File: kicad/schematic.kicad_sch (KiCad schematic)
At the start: 22 parts, among them J1 16X02 LCD Display I2C, J2 500g. Load Cell Sensor, J3 NAU7802, 24-Bit Dual-Channel.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, J4 TP4056 Lithium Battery Chargi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, SW1 Tare, SW2 Power Switch, SW3 Up, SW4 Down, SW5 Enter, SW6 Cancel, SW7 Coffee, U1 Step-up DC-to-DC 0.9-5V to 5V

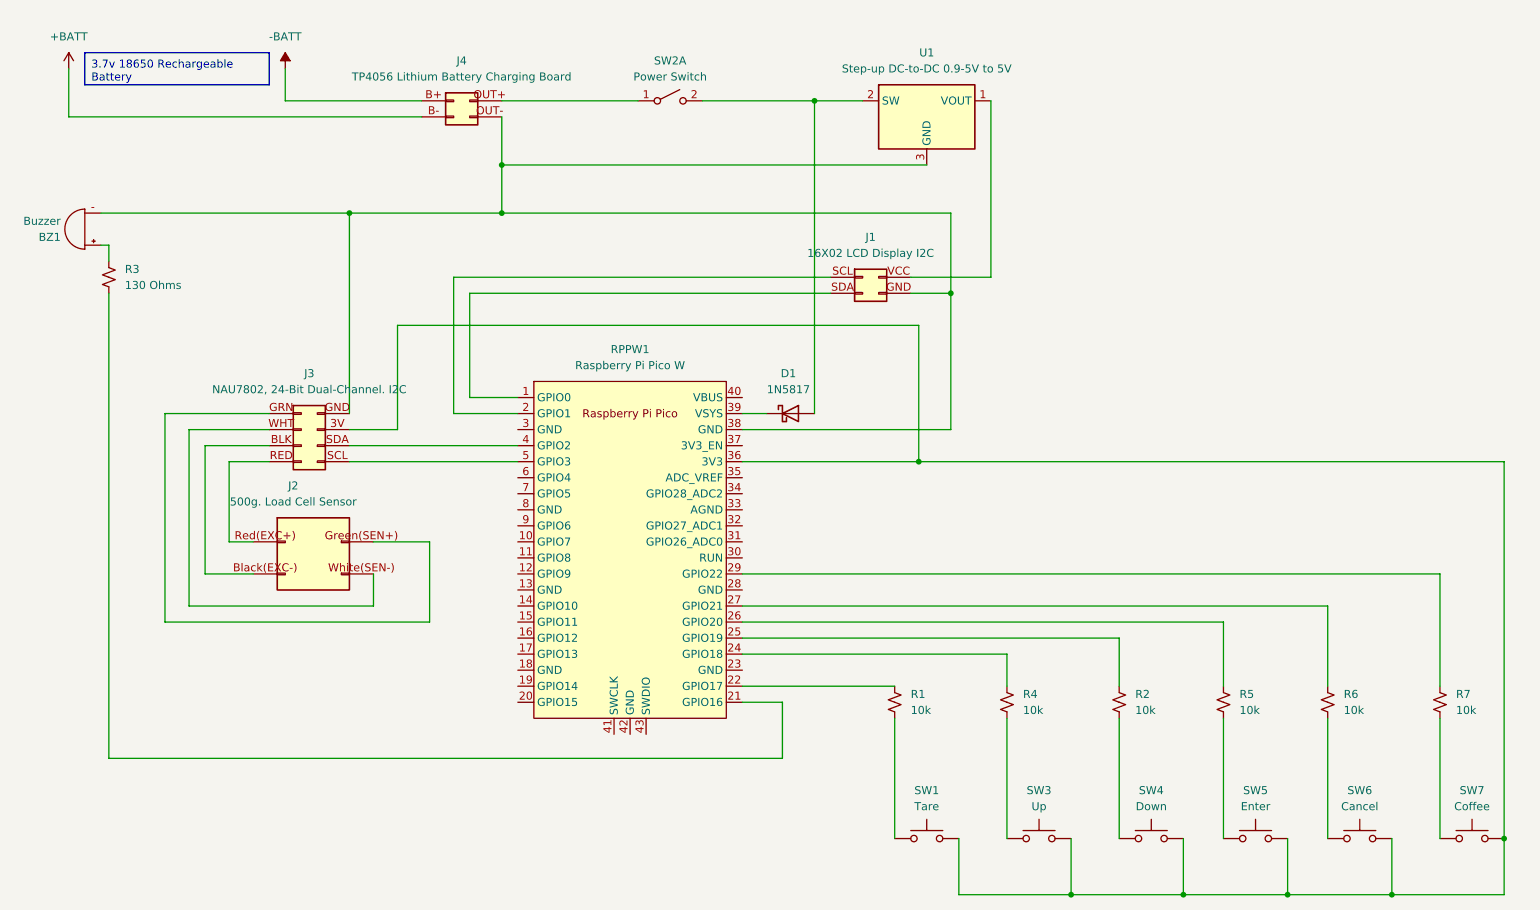
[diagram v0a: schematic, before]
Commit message: fix schematic buttons
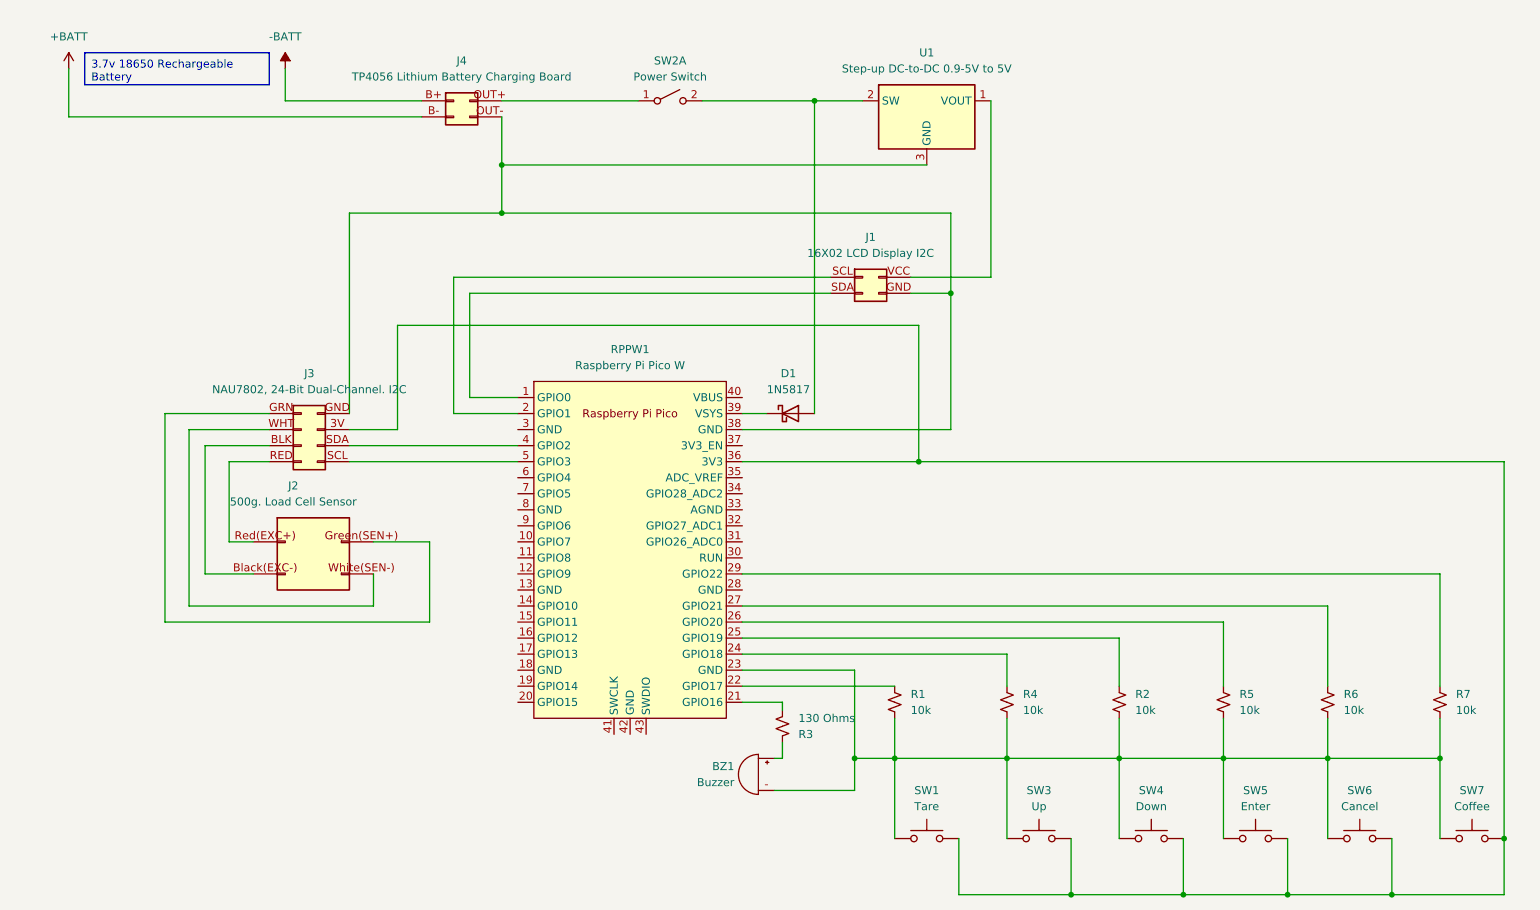
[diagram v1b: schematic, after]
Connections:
- net at J1.GND (Pin_3), J3.GND (Pin_8), J4.OUT- (Pin_3)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: no longer BZ1.-
- net at R2.2, SW4.1 (A), SW4.2 (A): now also BZ1.-, R1.2, R4.2, R5.2, R6.2, R7.2, RPPW1.23 (GND), SW1.1 (A), SW1.2 (A), SW3.1 (A), SW3.2 (A), SW5.1 (A), SW5.2 (A), SW6.1 (A), SW6.2 (A), SW7.1 (A), SW7.2 (A)
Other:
- moved on the sheet: BZ1, R3
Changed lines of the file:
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@@
   (junction (at 158.75 85.09) (diameter 0) (color 0 0 0 0)
   )
+  (junction (at 190.5 132.08) (diameter 0) (color 0 0 0 0)
+  )
+  (junction (at 241.3 132.08) (diameter 0) (color 0 0 0 0)
+  )
   (junction (at 182.88 153.67) (diameter 0) (color 0 0 0 0)
   )
+  (junction (at 207.01 132.08) (diameter 0) (color 0 0 0 0)
+  )
+  (junction (at 172.72 132.08) (diameter 0) (color 0 0 0 0)
+  )
+  (junction (at 154.94 132.08) (diameter 0) (color 0 0 0 0)
+  )
   (junction (at 92.71 38.1) (diameter 0) (color 0 0 0 0)
   )
@@
   (junction (at 217.17 153.67) (diameter 0) (color 0 0 0 0)
   )
-  (junction (at 68.58 45.72) (diameter 0) (color 0 0 0 0)
-  )
   (junction (at 251.46 144.78) (diameter 0) (color 0 0 0 0)
   )
+  (junction (at 148.59 132.08) (diameter 0) (color 0 0 0 0)
+  )
+  (junction (at 223.52 132.08) (diameter 0) (color 0 0 0 0)
+  )
   (junction (at 200.66 153.67) (diameter 0) (color 0 0 0 0)
   )
@@
     (stroke (width 0) (type default))
   )
+  (wire (pts (xy 172.72 132.08) (xy 172.72 144.78))
+    (stroke (width 0) (type default))
+  )
   (wire (pts (xy 223.52 107.95) (xy 130.81 107.95))
     (stroke (width 0) (type default))
@@
     (stroke (width 0) (type default))
   )
+  (wire (pts (xy 190.5 132.08) (xy 190.5 144.78))
+    (stroke (width 0) (type default))
+  )
   (wire (pts (xy 72.39 102.87) (xy 72.39 107.95))
     (stroke (width 0) (type default))
@@
     (stroke (width 0) (type default))
   )
+  (wire (pts (xy 148.59 118.11) (xy 148.59 132.08))
+    (stroke (width 0) (type default))
+  )
+  (wire (pts (xy 172.72 132.08) (xy 190.5 132.08))
+    (stroke (width 0) (type default))
+  )
+  (wire (pts (xy 241.3 125.73) (xy 241.3 132.08))
+    (stroke (width 0) (type default))
+  )
+  (wire (pts (xy 223.52 132.08) (xy 223.52 144.78))
+    (stroke (width 0) (type default))
+  )
   (wire (pts (xy 81.28 97.79) (xy 81.28 110.49))
     (stroke (width 0) (type default))
@@
     (stroke (width 0) (type default))
   )
-  (wire (pts (xy 30.48 58.42) (xy 30.48 132.08))
-    (stroke (width 0) (type default))
-  )
   (wire (pts (xy 130.81 115.57) (xy 172.72 115.57))
     (stroke (width 0) (type default))
@@
     (stroke (width 0) (type default))
   )
-  (wire (pts (xy 172.72 125.73) (xy 172.72 144.78))
+  (wire (pts (xy 172.72 125.73) (xy 172.72 132.08))
     (stroke (width 0) (type default))
   )
@@
     (stroke (width 0) (type default))
   )
+  (wire (pts (xy 148.59 132.08) (xy 154.94 132.08))
+    (stroke (width 0) (type default))
+  )
   (wire (pts (xy 92.71 38.1) (xy 92.71 45.72))
     (stroke (width 0) (type default))
@@
     (stroke (width 0) (type default))
   )
+  (wire (pts (xy 190.5 132.08) (xy 207.01 132.08))
+    (stroke (width 0) (type default))
+  )
   (wire (pts (xy 72.39 107.95) (xy 43.18 107.95))
     (stroke (width 0) (type default))
@@
     (stroke (width 0) (type default))
   )
-  (wire (pts (xy 154.94 125.73) (xy 154.94 144.78))
-    (stroke (width 0) (type default))
-  )
-  (wire (pts (xy 207.01 125.73) (xy 207.01 144.78))
-    (stroke (width 0) (type default))
-  )
-  (wire (pts (xy 223.52 125.73) (xy 223.52 144.78))
+  (wire (pts (xy 154.94 125.73) (xy 154.94 132.08))
+    (stroke (width 0) (type default))
+  )
+  (wire (pts (xy 207.01 125.73) (xy 207.01 132.08))
+    (stroke (width 0) (type default))
+  )
+  (wire (pts (xy 223.52 125.73) (xy 223.52 132.08))
     (stroke (width 0) (type default))
   )
@@
     (stroke (width 0) (type default))
   )
-  (wire (pts (xy 29.21 45.72) (xy 68.58 45.72))
+  (wire (pts (xy 223.52 132.08) (xy 241.3 132.08))
+    (stroke (width 0) (type default))
+  )
+  (wire (pts (xy 148.59 137.16) (xy 148.59 132.08))
+    (stroke (width 0) (type default))
+  )
+  (wire (pts (xy 207.01 132.08) (xy 223.52 132.08))
+    (stroke (width 0) (type default))
+  )
+  (wire (pts (xy 154.94 132.08) (xy 172.72 132.08))
     (stroke (width 0) (type default))
   )
@@
     (stroke (width 0) (type default))
   )
+  (wire (pts (xy 130.81 118.11) (xy 148.59 118.11))
+    (stroke (width 0) (type default))
+  )
   (wire (pts (xy 158.75 63.5) (xy 158.75 85.09))
     (stroke (width 0) (type default))
@@
     (stroke (width 0) (type default))
   )
-  (wire (pts (xy 190.5 125.73) (xy 190.5 144.78))
-    (stroke (width 0) (type default))
-  )
-  (wire (pts (xy 30.48 50.8) (xy 30.48 53.34))
+  (wire (pts (xy 190.5 125.73) (xy 190.5 132.08))
+    (stroke (width 0) (type default))
+  )
+  (wire (pts (xy 137.16 123.19) (xy 137.16 124.46))
+    (stroke (width 0) (type default))
+  )
+  (wire (pts (xy 137.16 132.08) (xy 137.16 129.54))
     (stroke (width 0) (type default))
   )
@@
     (stroke (width 0) (type default))
   )
-  (wire (pts (xy 241.3 125.73) (xy 241.3 144.78))
-    (stroke (width 0) (type default))
-  )
   (wire (pts (xy 241.3 120.65) (xy 241.3 102.87))
     (stroke (width 0) (type default))
@@
     (stroke (width 0) (type default))
   )
+  (wire (pts (xy 154.94 132.08) (xy 154.94 144.78))
+    (stroke (width 0) (type default))
+  )
   (wire (pts (xy 190.5 120.65) (xy 190.5 113.03))
     (stroke (width 0) (type default))
@@
     (stroke (width 0) (type default))
   )
-  (wire (pts (xy 137.16 132.08) (xy 137.16 123.19))
-    (stroke (width 0) (type default))
-  )
   (wire (pts (xy 85.09 55.88) (xy 85.09 77.47))
     (stroke (width 0) (type default))
@@
     (stroke (width 0) (type default))
   )
-  (wire (pts (xy 137.16 132.08) (xy 30.48 132.08))
-    (stroke (width 0) (type default))
-  )
   (wire (pts (xy 130.81 120.65) (xy 154.94 120.65))
     (stroke (width 0) (type default))
   )
+  (wire (pts (xy 135.89 137.16) (xy 148.59 137.16))
+    (stroke (width 0) (type default))
+  )
   (wire (pts (xy 24.13 22.86) (xy 24.13 30.48))
     (stroke (width 0) (type default))
@@
     (stroke (width 0) (type default))
   )
-  (wire (pts (xy 29.21 50.8) (xy 30.48 50.8))
+  (wire (pts (xy 135.89 132.08) (xy 137.16 132.08))
     (stroke (width 0) (type default))
   )
@@
     (stroke (width 0) (type default))
   )
+  (wire (pts (xy 207.01 132.08) (xy 207.01 144.78))
+    (stroke (width 0) (type default))
+  )
   (wire (pts (xy 142.24 27.94) (xy 142.24 77.47))
     (stroke (width 0) (type default))
   )
   (wire (pts (xy 137.16 123.19) (xy 130.81 123.19))
+    (stroke (width 0) (type default))
+  )
+  (wire (pts (xy 241.3 132.08) (xy 241.3 144.78))
     (stroke (width 0) (type default))
   )
@@
     )
   )
-  (symbol (lib_id "Device:R_Small_US") (at 30.48 55.88 0) (unit 1)
-    (in_bom yes) (on_board yes) (dnp no) (fields_autoplaced)
-    (property "Reference" "R3" (at 33.02 54.61 0)
-      (effects (font (size 1.27 1.27)) (justify left))
-    )
-    (property "Value" "130 Ohms" (at 33.02 57.15 0)
-      (effects (font (size 1.27 1.27)) (justify left))
-    )
-    (property "Footprint" "" (at 30.48 55.88 0)
-      (effects (font (size 1.27 1.27)) hide)
-    )
-    (property "Datasheet" "~" (at 30.48 55.88 0)
+  (symbol (lib_id "Device:R_Small_US") (at 137.16 127 0) (mirror x) (unit 1)
+    (in_bom yes) (on_board yes) (dnp no) (fields_autoplaced)
+    (property "Reference" "R3" (at 139.7 128.27 0)
+      (effects (font (size 1.27 1.27)) (justify left))
+    )
+    (property "Value" "130 Ohms" (at 139.7 125.73 0)
+      (effects (font (size 1.27 1.27)) (justify left))
+    )
+    (property "Footprint" "" (at 137.16 127 0)
+      (effects (font (size 1.27 1.27)) hide)
+    )
+    (property "Datasheet" "~" (at 137.16 127 0)
       (effects (font (size 1.27 1.27)) hide)
     )
@@
     )
   )
-  (symbol (lib_id "Device:Buzzer") (at 26.67 48.26 180) (unit 1)
+  (symbol (lib_id "Device:Buzzer") (at 133.35 134.62 0) (mirror y) (unit 1)
     (in_bom yes) (on_board yes) (dnp no)
-    (property "Reference" "BZ1" (at 22.86 49.53 0)
-      (effects (font (size 1.27 1.27)) (justify left))
-    )
-    (property "Value" "Buzzer" (at 22.86 46.99 0)
-      (effects (font (size 1.27 1.27)) (justify left))
-    )
-    (property "Footprint" "" (at 27.305 50.8 90)
-      (effects (font (size 1.27 1.27)) hide)
-    )
-    (property "Datasheet" "~" (at 27.305 50.8 90)
-      (effects (font (size 1.27 1.27)) hide)
-    )
+    (property "Reference" "BZ1" (at 129.54 133.35 0)
+      (effects (font (size 1.27 1.27)) (justify left))
+    )
+    (property "Value" "Buzzer" (at 129.54 135.89 0)
+      (effects (font (size 1.27 1.27)) (justify left))
+    )
+    (property "Footprint" "" (at 133.985 132.08 90)
+      (effects (font (size 1.27 1.27)) hide)
+    )
+    (property "Datasheet" "~" (at 133.985 132.08 90)
+      (effects (font (size 1.27 1.27)) hide)
+    )

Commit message: add soft switch
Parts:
- removed SW2: Power Switch, symbol Switch:SW_DPST_x2
- added J5: Soft Power Switch: SPX-17870, symbol Connector_Generic:Conn_2Rows-07Pins
- added Q1: PN2222A, Package_TO_SOT_THT:TO-92_Inline, symbol Transistor_BJT:PN2222A
- added R8: 220 Ω, symbol Device:R_Small_US
- added R9: 10 KΩ, symbol Device:R_Small_US
- added SW2: Power, symbol Switch:SW_MEC_5G
- R1, R2, R4, R5, R6, R7: value 10k -> 10kΩ
- R3: value 130 Ohms -> 120 Ω
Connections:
- net at D1.2 (A), U1.2 (SW): now also J5.SYS_+ (Pin_3)
- net at J1.GND (Pin_3), J3.GND (Pin_8), J4.OUT- (Pin_3)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: now also J5.BATT_- (Pin_7), J5.SYS_- (Pin_1), Q1.1 (E), SW2.3 (B), SW2.4 (B)
- net at J4.OUT+ (4): now also J5.BATT_+ (Pin_5)
- net at RPPW1.19 (GPIO14): now also J5.SEN/CTRL
- net at RPPW1.20 (GPIO15): now also R8.1
- new net: Q1.2 (B), R8.2
- new net: J5.BTN (Pin_2), SW2.1 (A), SW2.2 (A)
- new net: J5.FASTOFF (Pin_6), R9.1
- new net: Q1.3 (C), R9.2
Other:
- moved on the sheet: U1

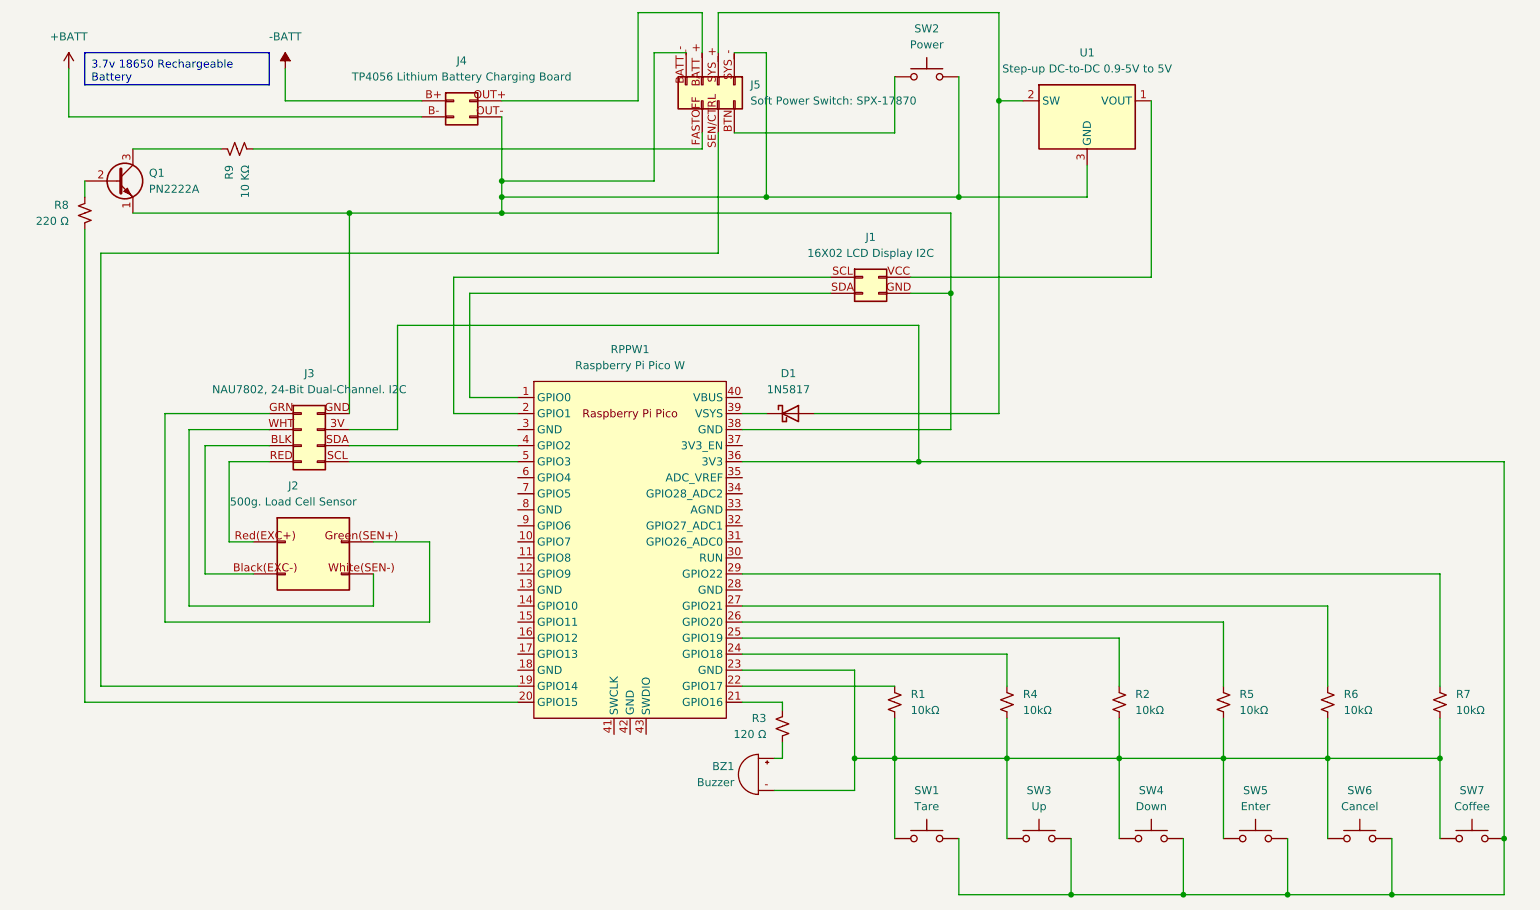
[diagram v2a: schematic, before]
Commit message: fix(schematic): buttons
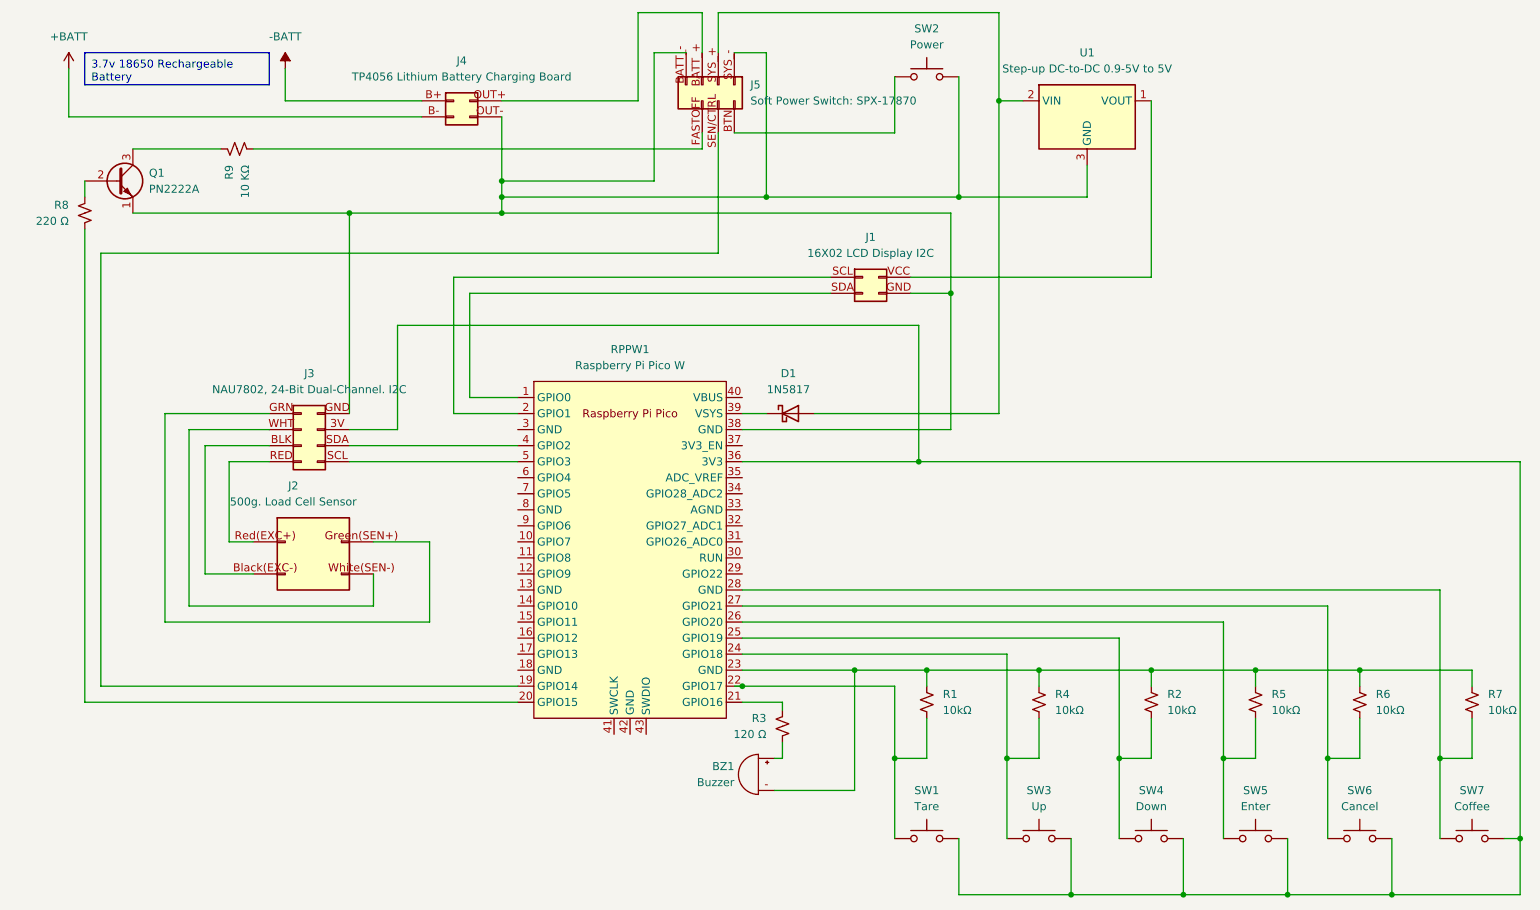
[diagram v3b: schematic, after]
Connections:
- net at R2.1: now also BZ1.-, R1.1, R4.1, R5.1, R6.1, R7.1, RPPW1.23 (GND); no longer RPPW1.25 (GPIO19)
- net at RPPW1.24 (GPIO18): now also R4.2, SW3.1 (A), SW3.2 (A); no longer R4.1
- net at RPPW1.29 (GPIO22): no longer R7.1
- net at RPPW1.26 (GPIO20): now also R5.2, SW5.1 (A), SW5.2 (A); no longer R5.1
- net at RPPW1.22 (GPIO17): now also R1.2, SW1.1 (A), SW1.2 (A); no longer R1.1
- net at RPPW1.27 (GPIO21): now also R6.2, SW6.1 (A), SW6.2 (A); no longer R6.1
- net at RPPW1.28 (GND): now also R7.2, SW7.1 (A), SW7.2 (A)
- new net: R2.2, RPPW1.25 (GPIO19), SW4.1 (A), SW4.2 (A)
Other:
- moved on the sheet: R1, R2, R4, R5, R6, R7
